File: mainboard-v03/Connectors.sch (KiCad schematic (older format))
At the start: 13 parts, among them J1 503182-1852, J2 Conn_01x05, J3 10118194-0001LF, J4 DCJ0303, U8 MR25H40MDF

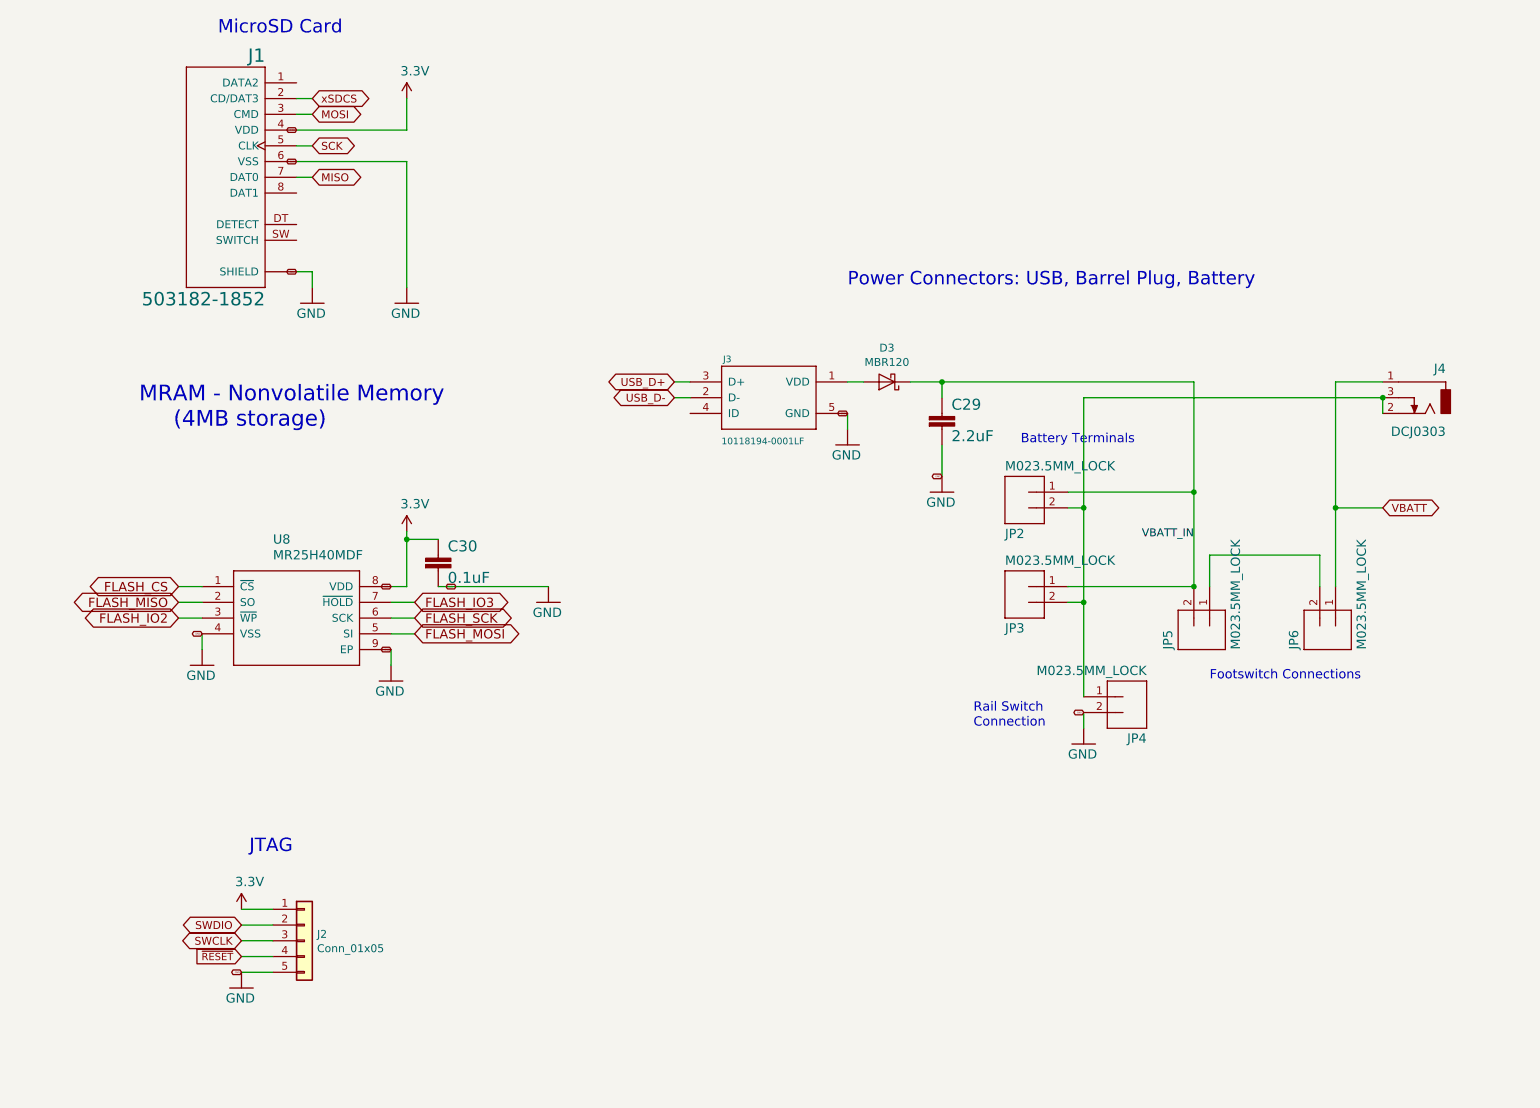
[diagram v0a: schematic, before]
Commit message: cleaning up schematic scheets
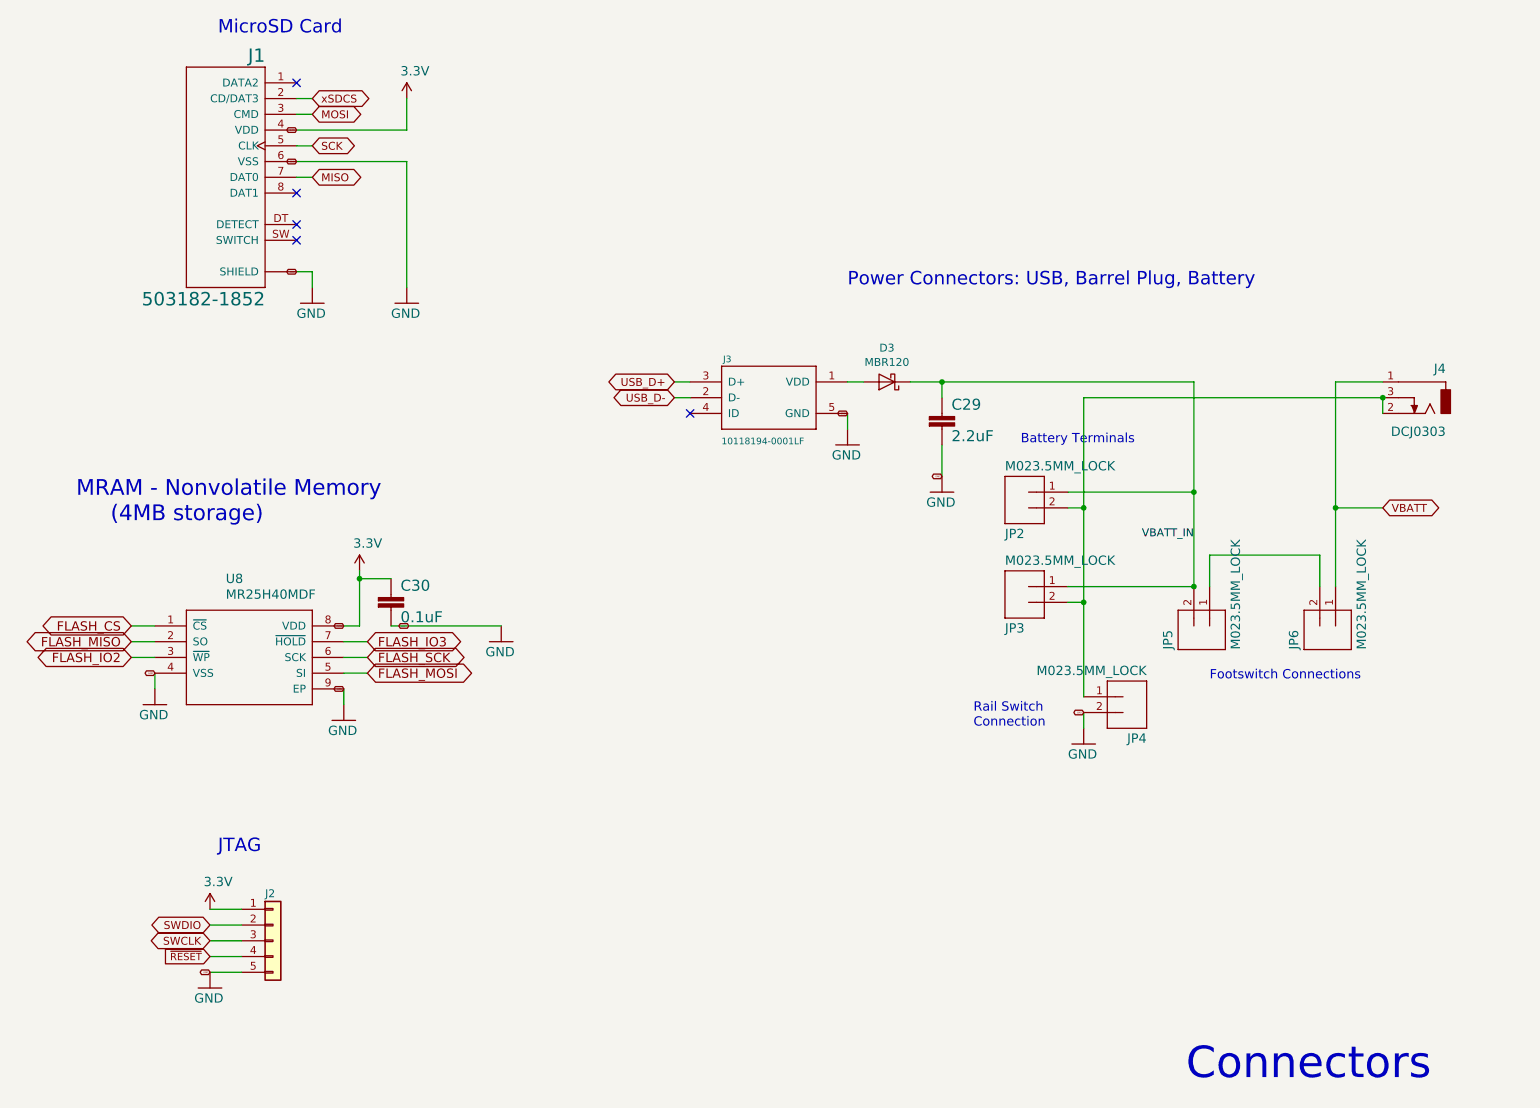
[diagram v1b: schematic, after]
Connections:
- no-connect marks 0 -> 5
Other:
- note added: "Connectors"
- moved on the sheet: C30, J2, U8
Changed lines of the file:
@@
 Title "PyCubed Mainboard"
 Date ""
-Rev "v02"
+Rev "v03"
 Comp "Stanford University"
 Comment1 "rexlab.stanford.edu"
@@
 GND
 Wire Wire Line
-	2300 4700 2300 4800
-Text GLabel 2300 4700 0    10   BiDi ~ 0
-GND
-Wire Wire Line
-	3500 4800 3500 4900
-Text GLabel 3500 4800 0    10   BiDi ~ 0
+	2000 4950 2000 5050
+Text GLabel 2000 4950 0    10   BiDi ~ 0
+GND
+Wire Wire Line
+	3200 5050 3200 5150
+Text GLabel 3200 5050 0    10   BiDi ~ 0
 GND
 Wire Wire Line
@@
 3.3V
 Wire Wire Line
-	3500 4400 3600 4400
-Wire Wire Line
-	3600 4400 3600 4100
-Text GLabel 3500 4400 0    10   BiDi ~ 0
+	3200 4650 3300 4650
+Wire Wire Line
+	3300 4650 3300 4350
+Text GLabel 3200 4650 0    10   BiDi ~ 0
 3.3V
-Text GLabel 2550 6650 0    50   BiDi ~ 0
+Text GLabel 2350 6650 0    50   BiDi ~ 0
 SWCLK
-Text GLabel 2550 6550 0    50   BiDi ~ 0
+Text GLabel 2350 6550 0    50   BiDi ~ 0
 SWDIO
 Wire Wire Line
@@
 L mainboard:MR25H40MDF U?
 U 1 0 4AD49080
-P 2300 4400
+P 2000 4650
 AR Path="/4AD49080" Ref="U?"  Part="1"
 AR Path="/5CEC60EB/4AD49080" Ref="U8"  Part="1"
-F 0 "U8" H 2750 4700 59  0000 L CNN
-F 1 "MR25H40MDF" H 2750 4600 59  0000 L CNN
-F 2 "kmb-test:SON127P600X500X90-9N" H 2300 4400 50  0001 C CNN
-F 3 "" H 2300 4400 50  0001 C CNN
-	1    2300 4400
+F 0 "U8" H 2450 4950 59  0000 L CNN
+F 1 "MR25H40MDF" H 2450 4850 59  0000 L CNN
+F 2 "kmb-test:SON127P600X500X90-9N" H 2000 4650 50  0001 C CNN
+F 3 "" H 2000 4650 50  0001 C CNN
+	1    2000 4650
 	1    0    0    -1
 $EndComp
@@
 L mainboard:3.3V #SUPPLY?
 U 1 0 8D803956
-P 3600 4050
+P 3300 4300
 AR Path="/8D803956" Ref="#SUPPLY?"  Part="1"
 AR Path="/5CEC60EB/8D803956" Ref="#SUPPLY08"  Part="1"
-F 0 "#SUPPLY08" H 3600 4050 50  0001 C CNN
-F 1 "3.3V" H 3560 4190 59  0000 L BNN
-F 2 "" H 3600 4050 50  0001 C CNN
-F 3 "" H 3600 4050 50  0001 C CNN
-	1    3600 4050
+F 0 "#SUPPLY08" H 3300 4300 50  0001 C CNN
+F 1 "3.3V" H 3260 4440 59  0000 L BNN
+F 2 "" H 3300 4300 50  0001 C CNN
+F 3 "" H 3300 4300 50  0001 C CNN
+	1    3300 4300
 	1    0    0    -1
 $EndComp
@@
 L mainboard:GND #GND?
 U 1 0 057C4BD5
-P 2300 4900
+P 2000 5150
 AR Path="/057C4BD5" Ref="#GND?"  Part="1"
 AR Path="/5CEC60EB/057C4BD5" Ref="#GND022"  Part="1"
-F 0 "#GND022" H 2300 4900 50  0001 C CNN
-F 1 "GND" H 2200 4800 59  0000 L BNN
-F 2 "" H 2300 4900 50  0001 C CNN
-F 3 "" H 2300 4900 50  0001 C CNN
-	1    2300 4900
+F 0 "#GND022" H 2000 5150 50  0001 C CNN
+F 1 "GND" H 1900 5050 59  0000 L BNN
+F 2 "" H 2000 5150 50  0001 C CNN
+F 3 "" H 2000 5150 50  0001 C CNN
+	1    2000 5150
 	1    0    0    -1
 $EndComp
@@
 L mainboard:GND #GND?
 U 1 0 6D21A43A
-P 3500 5000
+P 3200 5250
 AR Path="/6D21A43A" Ref="#GND?"  Part="1"
 AR Path="/5CEC60EB/6D21A43A" Ref="#GND025"  Part="1"
-F 0 "#GND025" H 3500 5000 50  0001 C CNN
-F 1 "GND" H 3400 4900 59  0000 L BNN
-F 2 "" H 3500 5000 50  0001 C CNN
-F 3 "" H 3500 5000 50  0001 C CNN
-	1    3500 5000
+F 0 "#GND025" H 3200 5250 50  0001 C CNN
+F 1 "GND" H 3100 5150 59  0000 L BNN
+F 2 "" H 3200 5250 50  0001 C CNN
+F 3 "" H 3200 5250 50  0001 C CNN
+	1    3200 5250
 	1    0    0    -1
 $EndComp
@@
 Text Notes 7200 5300 0    59   ~ 0
 Rail Switch\nConnection
-Text Notes 2600 6100 0    85   ~ 0
+Text Notes 2400 6100 0    85   ~ 0
 JTAG
 Text Notes 6400 2500 0    85   ~ 0
@@
 Text Notes 2400 900  0    85   ~ 0
 MicroSD Card
-Text Notes 1900 3400 0    100  ~ 0
+Text Notes 1500 4000 0    100  ~ 0
 MRAM - Nonvolatile Memory\n     (4MB storage)
 $Comp
@@
 Connection ~ 7000 3100
 Wire Wire Line
-	2550 6450 2750 6450
-Text GLabel 2550 6850 0    10   BiDi ~ 0
+	2350 6450 2550 6450
+Text GLabel 2350 6850 0    10   BiDi ~ 0
 GND
 $Comp
 L mainboard:GND #GND?
 U 1 0 5D35314F
-P 2550 6950
+P 2350 6950
 AR Path="/5D35314F" Ref="#GND?"  Part="1"
 AR Path="/5CEC60EB/5D35314F" Ref="#GND023"  Part="1"
-F 0 "#GND023" H 2550 6950 50  0001 C CNN
-F 1 "GND" H 2450 6850 59  0000 L BNN
-F 2 "" H 2550 6950 50  0001 C CNN
-F 3 "" H 2550 6950 50  0001 C CNN
-	1    2550 6950
-	1    0    0    -1
-$EndComp
-Wire Wire Line
-	2550 6850 2750 6850
+F 0 "#GND023" H 2350 6950 50  0001 C CNN
+F 1 "GND" H 2250 6850 59  0000 L BNN
+F 2 "" H 2350 6950 50  0001 C CNN
+F 3 "" H 2350 6950 50  0001 C CNN
+	1    2350 6950
+	1    0    0    -1
+$EndComp
+Wire Wire Line
+	2350 6850 2550 6850
 $Comp
 L Connector_Generic:Conn_01x05 J2
 U 1 1 5D355CD9
-P 2950 6650
-F 0 "J2" H 3030 6692 50  0000 L CNN
-F 1 "Conn_01x05" H 3030 6601 50  0000 L CNN
-F 2 "Connector_PinHeader_2.54mm:PinHeader_1x05_P2.54mm_Vertical" H 2950 6650 50  0001 C CNN
-F 3 "~" H 2950 6650 50  0001 C CNN
-	1    2950 6650
-	1    0    0    -1
-$EndComp
-Text GLabel 2550 6750 0    46   Input ~ 0
+P 2750 6650
+F 0 "J2" H 2700 6950 50  0000 L CNN
+F 1 "Conn_01x05" H 2830 6601 50  0001 L CNN
+F 2 "Connector_PinHeader_2.54mm:PinHeader_1x05_P2.54mm_Vertical" H 2750 6650 50  0001 C CNN
+F 3 "~" H 2750 6650 50  0001 C CNN
+	1    2750 6650
+	1    0    0    -1
+$EndComp
+Text GLabel 2350 6750 0    46   Input ~ 0
 ~RESET
 Wire Wire Line
-	2750 6550 2550 6550
-Wire Wire Line
-	2750 6650 2550 6650
-Wire Wire Line
-	2750 6750 2550 6750
-Text GLabel 2150 4500 0    59   BiDi ~ 0
+	2550 6550 2350 6550
+Wire Wire Line
+	2550 6650 2350 6650
+Wire Wire Line
+	2550 6750 2350 6750
+Text GLabel 1850 4750 0    59   BiDi ~ 0
 FLASH_MISO
 Wire Wire Line
-	2150 4500 2300 4500
-Text GLabel 2150 4400 0    59   BiDi ~ 0
+	1850 4750 2000 4750
+Text GLabel 1850 4650 0    59   BiDi ~ 0
 FLASH_CS
-Text GLabel 3650 4600 2    59   BiDi ~ 0
+Text GLabel 3350 4850 2    59   BiDi ~ 0
 FLASH_SCK
 Wire Wire Line
-	3650 4600 3500 4600
-Wire Wire Line
-	2150 4400 2300 4400
-Wire Wire Line
-	3650 4700 3500 4700
-Text GLabel 3650 4700 2    59   BiDi ~ 0
+	3350 4850 3200 4850
+Wire Wire Line
+	1850 4650 2000 4650
+Wire Wire Line
+	3350 4950 3200 4950
+Text GLabel 3350 4950 2    59   BiDi ~ 0
 FLASH_MOSI
 $Comp
 L mainboard:2.2UF-0603-10V-20% C?
 U 1 0 5D3374E2
-P 3800 4300
+P 3500 4550
 AR Path="/5D3374E2" Ref="C?"  Part="1"
 AR Path="/5CEC60EB/5D3374E2" Ref="C30"  Part="1"
-F 0 "C30" H 3860 4415 70  0000 L BNN
-F 1 "0.1uF" H 3860 4215 70  0000 L BNN
-F 2 "Capacitor_SMD:C_0603_1608Metric" H 3800 4300 50  0001 C CNN
-F 3 "" H 3800 4300 50  0001 C CNN
-	1    3800 4300
-	1    0    0    -1
-$EndComp
-Wire Wire Line
-	3800 4100 3600 4100
-Connection ~ 3600 4100
-Wire Wire Line
-	3600 4100 3600 4050
-Wire Wire Line
-	3800 4400 4500 4400
+F 0 "C30" H 3560 4665 70  0000 L BNN
+F 1 "0.1uF" H 3560 4465 70  0000 L BNN
+F 2 "Capacitor_SMD:C_0603_1608Metric" H 3500 4550 50  0001 C CNN
+F 3 "" H 3500 4550 50  0001 C CNN
+	1    3500 4550
+	1    0    0    -1
+$EndComp
+Wire Wire Line
+	3500 4350 3300 4350
+Connection ~ 3300 4350
+Wire Wire Line
+	3300 4350 3300 4300
+Wire Wire Line
+	3500 4650 4200 4650
 $Comp
 L mainboard:GND #GND?
 U 1 0 5D33B931
-P 4500 4500
+P 4200 4750
 AR Path="/5D33B931" Ref="#GND?"  Part="1"
 AR Path="/5CEC60EB/5D33B931" Ref="#GND065"  Part="1"
-F 0 "#GND065" H 4500 4500 50  0001 C CNN
-F 1 "GND" H 4400 4400 59  0000 L BNN
-F 2 "" H 4500 4500 50  0001 C CNN
-F 3 "" H 4500 4500 50  0001 C CNN
-	1    4500 4500
-	1    0    0    -1
-$EndComp
-Text GLabel 3850 4400 2    10   BiDi ~ 0
+F 0 "#GND065" H 4200 4750 50  0001 C CNN
+F 1 "GND" H 4100 4650 59  0000 L BNN
+F 2 "" H 4200 4750 50  0001 C CNN
+F 3 "" H 4200 4750 50  0001 C CNN
+	1    4200 4750
+	1    0    0    -1
+$EndComp
+Text GLabel 3550 4650 2    10   BiDi ~ 0
 GND
 $Comp
 L mainboard:3.3V #SUPPLY?
 U 1 0 5D35C898
-P 2550 6450
+P 2350 6450
 AR Path="/5D35C898" Ref="#SUPPLY?"  Part="1"
 AR Path="/5CEC60EB/5D35C898" Ref="#SUPPLY0102"  Part="1"
-F 0 "#SUPPLY0102" H 2550 6450 50  0001 C CNN
-F 1 "3.3V" H 2510 6590 59  0000 L BNN
-F 2 "" H 2550 6450 50  0001 C CNN
-F 3 "" H 2550 6450 50  0001 C CNN
-	1    2550 6450
-	1    0    0    -1
-$EndComp
-Text GLabel 3650 4500 2    59   BiDi ~ 0
+F 0 "#SUPPLY0102" H 2350 6450 50  0001 C CNN
+F 1 "3.3V" H 2310 6590 59  0000 L BNN
+F 2 "" H 2350 6450 50  0001 C CNN
+F 3 "" H 2350 6450 50  0001 C CNN
+	1    2350 6450
+	1    0    0    -1
+$EndComp
+Text GLabel 3350 4750 2    59   BiDi ~ 0
 FLASH_IO3
 Wire Wire Line
-	3650 4500 3500 4500
-Text GLabel 2150 4600 0    59   BiDi ~ 0
+	3350 4750 3200 4750
+Text GLabel 1850 4850 0    59   BiDi ~ 0
 FLASH_IO2
 Wire Wire Line
-	2150 4600 2300 4600
+	1850 4850 2000 4850
+Text Notes 8550 7550 0    200  ~ 0
+Connectors
+NoConn ~ 5400 3300
+NoConn ~ 2900 1900
+NoConn ~ 2900 2100
+NoConn ~ 2900 2200
+NoConn ~ 2900 1200
 $EndSCHEMATC

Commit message: mainboardv3 clean up
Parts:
- removed C29: 2.2uF, Capacitor_SMD:C_0603_1608Metric, symbol mainboard:2.2UF-0603-10V-20%
- removed D3: MBR120, custom-footprints:D_SOD-123, symbol Diode:MBR340
- removed J3: 10118194-0001LF, kmb-test:FRAMATOME_10118194-0001LF, symbol mainboard:10118194-0001LF
- removed J4: DCJ0303, kmb-test:DCJ0303, symbol mainboard:DCJ0303
- added C24: 0.1uF, Capacitor_SMD:C_0603_1608Metric, symbol Device:C_Small
- added C29: 4.7uF, Capacitor_SMD:C_0603_1608Metric, symbol Device:C_Small
- added C31: 22uF, Capacitor_SMD:C_0603_1608Metric, symbol Device:C_Small
- added D3: ESDA25P35, custom-footprints:ESDA8P801U1M, symbol Device:D_TVS
- added J13: USB_C_Receptacle_USB2.0, custom-footprints:USB_C_Receptacle_XKB_U262-161N-4BVC11, symbol Connector:USB_C_Receptacle_USB2.0
- added J3: Conn_01x01, Connector_PinHeader_2.54mm:PinHeader_1x01_P2.54mm_Vertical, symbol Connector_Generic:Conn_01x01
- added J4: 10118194-0001LF, custom-footprints:10118194-0001LF, symbol 10118194-0001LF:10118194-0001LF
- added R39, R40: 5.1k, Resistor_SMD:R_0603_1608Metric, symbol Device:R_US
- J1: footprint kmb-test:MOLEX_503182-1852 -> mainboard:MOLEX_503182-1852
- JP2, JP3, JP4, JP5, JP6: footprint kmb-test:SCREWTERMINAL-3.5MM-2_LOCK -> mainboard:SCREWTERMINAL-3.5MM-2_LOCK
- U8: footprint kmb-test:SON127P600X500X90-9N -> mainboard:SON127P600X500X90-9N; Flight (none) -> MR25H40MDF; Proto (none) -> W25Q80DVSNIG
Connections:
- net USB_D+: now also J13.A6 (D+), J13.B6 (D+), J4.3 (D+)
- net USB_D-: now also J13.A7 (D-), J13.B7 (D-), J4.2 (D-)
- net GNDREF: now reaches JP2.2, JP3.2, JP4.1
- net GNDREF: now also C24.2, C29.2, C31.2, D3.1 (A1), J13.A1 (GND), J13.A12 (GND), J13.B1 (GND), J13.B12 (GND), J13.S1 (SHIELD), J4.5 (GND), J4.8, J4.9 (SHIELD), R39.1, R40.1
- net VBATT_IN renamed VCHRG
- net VCHRG: now also C24.1, C31.1
- new net THM: J3.1 (Pin_1)
- new net USB_CC1: J13.A5 (CC1), R40.2
- new net USB_CC2: J13.B5 (CC2), R39.2
- new net VBUS_IN: C29.1, D3.2 (A2), J13.A4 (VBUS), J13.A9 (VBUS), J13.B4 (VBUS), J13.B9 (VBUS), J4.1 (VDD)
- no-connect marks 5 -> 7
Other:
- note added: "Battery Thermal \nMonitor (optional)"
- note added: "Power Connectors: USB-C Power Delivery to 2S Li-ion Battery"
- note removed: "Power Connectors: USB, Barrel Plug, Battery"
